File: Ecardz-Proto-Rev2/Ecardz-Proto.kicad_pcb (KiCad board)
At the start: 4 copper layers, 53.2 x 93.2 mm, 66 parts, among them IC1 M24LR04E-RMN6T/2, J2 Conn_01x24, J3 Conn_01x06, Q1 NMOS, U1 STM32L071K8Ux

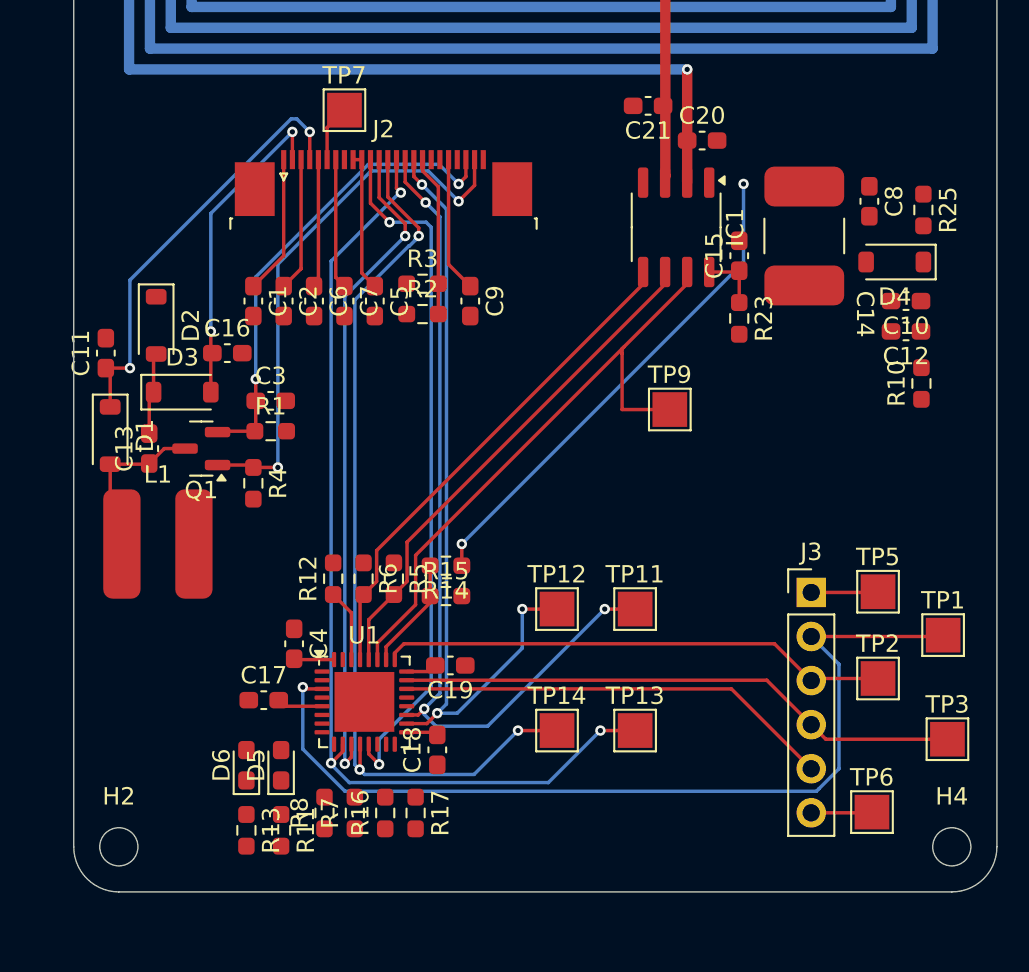
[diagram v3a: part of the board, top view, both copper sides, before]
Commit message: Added traces for everything but gruond layer
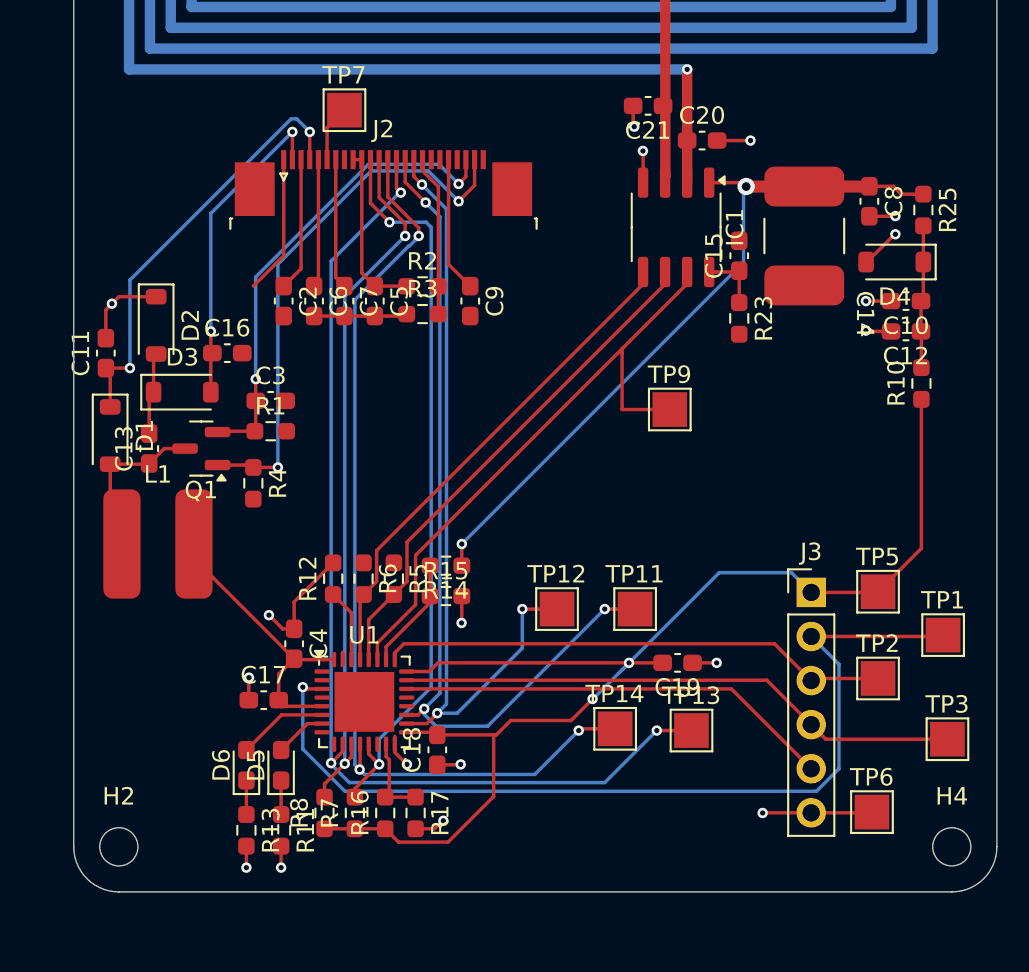
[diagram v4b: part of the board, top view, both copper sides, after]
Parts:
- removed C1: 1uF, Capacitor_SMD:C_0603_1608Metric_Pad1.08x0.95mm_HandSolder
- moved C19 13.1 mm to (193.2, 102.6)
- moved TP14 3.35 mm to (189.6, 106.4)
- moved TP13 3.25 mm to (194.0, 106.5)
- moved R3 1.75 mm to (178.5, 82.5)
- moved R2 1.60 mm to (178.5, 80.9)
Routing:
- net VDD: track 20.1 -> 100.4 mm, vias 0 -> 2
- net GND: track 3.52 -> 50.2 mm, vias 0 -> 18
- net /NFC/V_E_HARVEST: track 28.7 -> 41.3 mm
- net VDD_HARVEST: track 0.00 -> 8.24 mm
- net /STM/INDICATOR_R: track 0.00 -> 5.20 mm
- net /STM/VDD_MEAS: track 0.00 -> 4.97 mm
- net /EINK/CS#: track 51.6 -> 55.0 mm
- net /EINK/D/C#: track 57.2 -> 60.5 mm
- net /STM/INDICATOR_G: track 0.00 -> 2.99 mm
- net /EINK/SDA: track 40.2 -> 42.7 mm
- net /EINK/SCL: track 38.2 -> 40.6 mm
- net Net-(D6-K): track 0.00 -> 1.96 mm
- net Net-(D5-K): track 0.00 -> 1.96 mm
- added copper zone on In1.Cu, net GND

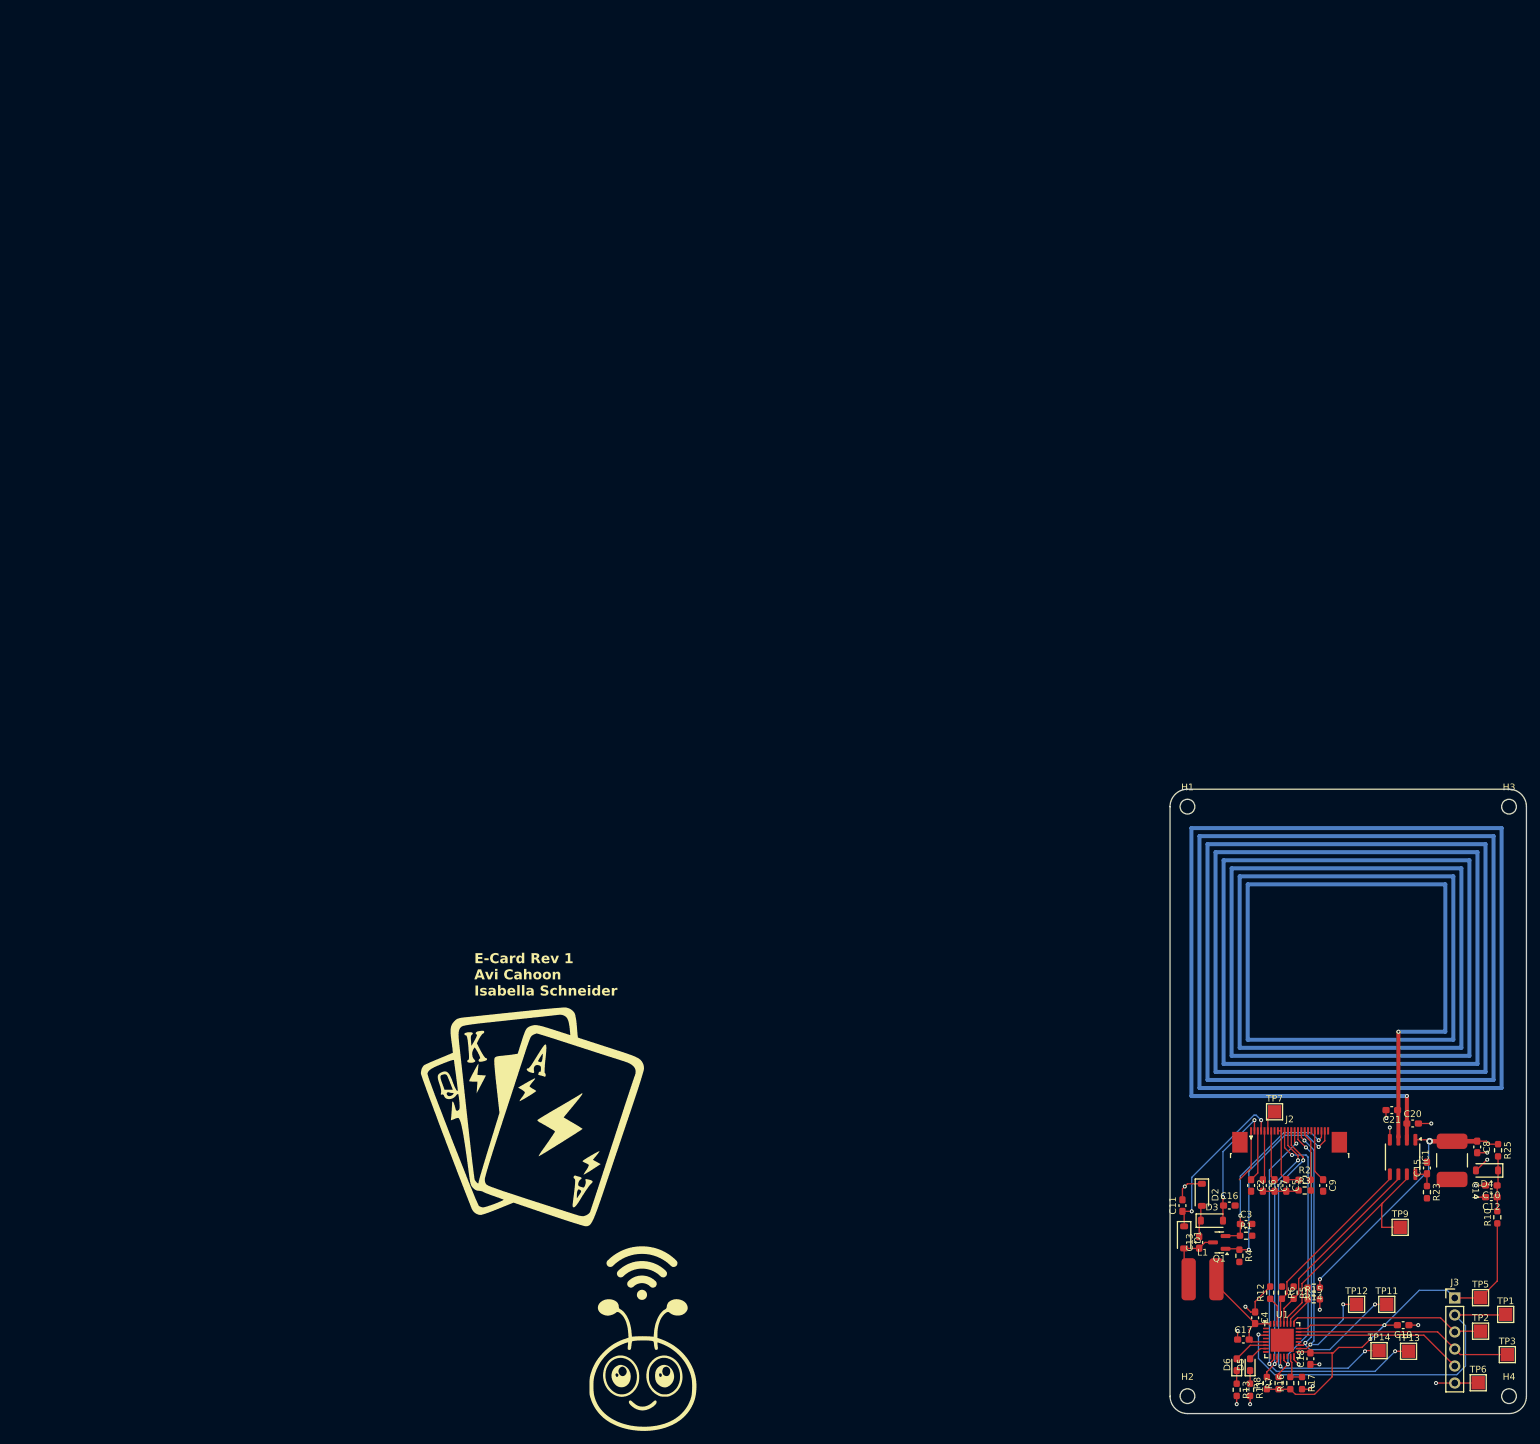
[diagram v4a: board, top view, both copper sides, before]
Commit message: Finished all layout, need to fix inductor and capacitor library
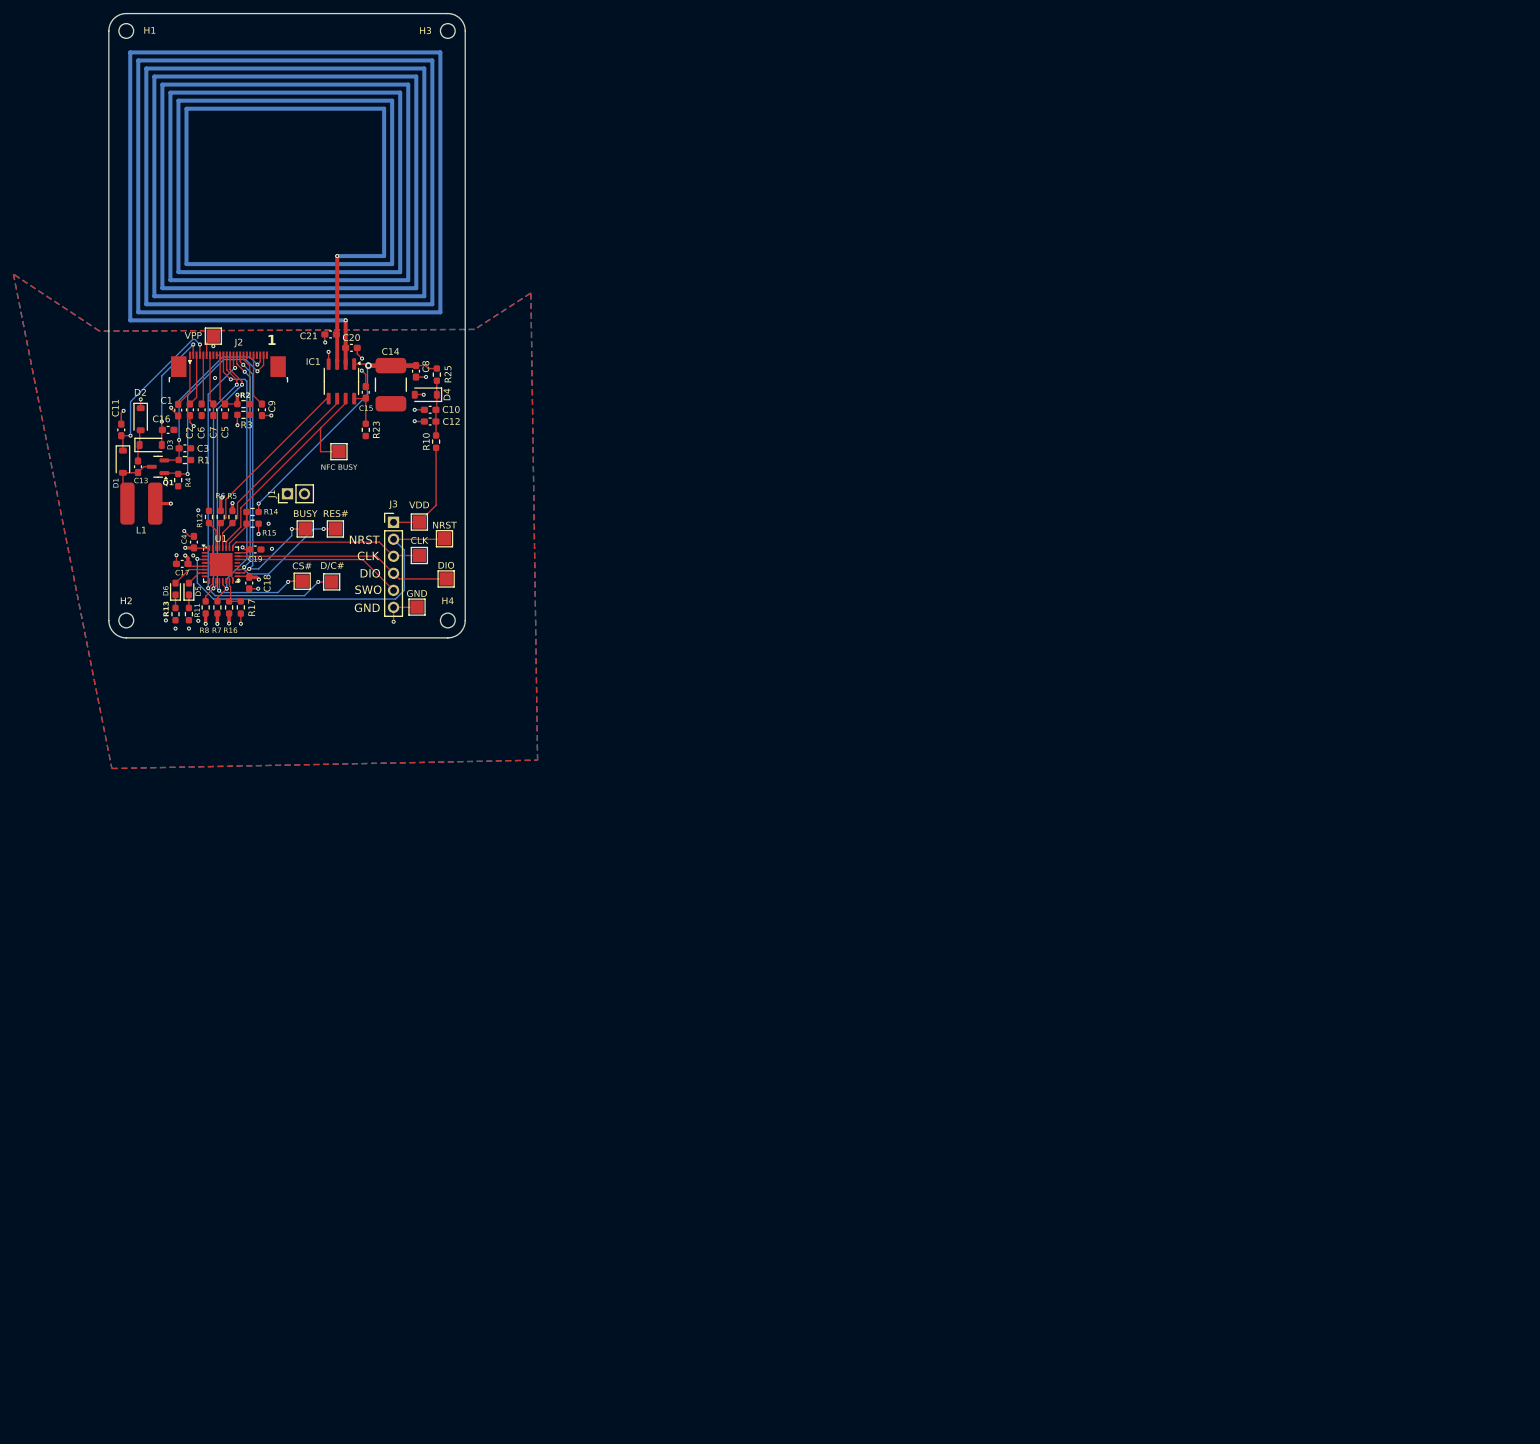
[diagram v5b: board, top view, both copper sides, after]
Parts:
- added C1: 1uF, Capacitor_SMD:C_0603_1608Metric_Pad1.08x0.95mm_HandSolder, F.Cu at (10.3, -34.0)
- added J1: Conn_01x02, Connector_PinHeader_2.54mm:PinHeader_1x02_P2.54mm_Vertical, F.Cu at (26.6, -21.5)
- NFC BUSY: renamed from TP9
- moved C19 206.8 mm to (21.8, -13.2)
- moved CS# 197.6 mm to (28.9, -8.45)
- moved D/C# 197.6 mm to (33.2, -8.35)
- moved C10 196.2 mm to (48.0, -34.0)
- moved C12 196.2 mm to (48.0, -32.3)
- moved C20 196.2 mm to (36.2, -43.3)
- moved D2 196.2 mm to (4.74, -32.6)
- moved D3 196.2 mm to (6.24, -28.8)
- moved IC1 196.2 mm to (34.7, -38.3)
- moved R25 196.2 mm to (49.0, -39.3)
- moved C11 196.2 mm to (1.84, -31.0)
- moved C13 196.2 mm to (4.34, -25.5)
- moved C14 196.2 mm to (42.1, -37.8)
- moved C15 196.2 mm to (38.3, -36.7)
- moved C16 196.2 mm to (8.84, -31.0)
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- renumbered TP12 to BUSY, TP2 to CLK, TP14 to CS#, TP13 to D/C#, TP3 to DIO, TP6 to GND, TP1 to NRST, TP11 to RES#, TP5 to VDD, TP7 to VPP
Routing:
- net VDD: track 100.4 -> 53.1 mm, vias 2 -> 11
- net GND: track 50.2 -> 47.3 mm, vias 18 -> 31
- net /EINK/D/C#: track 60.5 -> 57.8 mm
- net /EINK/CS#: track 55.0 -> 52.3 mm
- net /NFC/VDD_NFC: track 3.60 -> 5.60 mm
- net /EINK/RES#: track 49.6 -> 51.0 mm
- net /EINK/BUSY: track 45.6 -> 46.3 mm
- added copper zone on B.Cu, net GND
- added copper zone on F.Cu, net GND
- added copper zone on In2.Cu, net VDD
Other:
- board text added: "1"
- board text added: "CLK"
- board text added: "DIO"
- board text added: "GND"
- board text added: "NRST"
- board text added: "SWO"
- board text removed: "E-Card Rev 1 Avi Cahoon Isabella Schneider"

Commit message: final schematic
final schematic done and BOM generated except for pogo pins and capacitors
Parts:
- removed the C8 at (45.8, -39.8)
- added C22: TBD, parts-lib:C_2917, F.Cu at (46.5, -38.0)
- added C23: TBD, Capacitor_SMD:C_0805_2012Metric_Pad1.18x1.45mm_HandSolder, F.Cu at (34.8, -40.2)
- added C8: TBD, Capacitor_SMD:C_0805_2012Metric_Pad1.18x1.45mm_HandSolder, F.Cu at (51.8, -31.0)
- added C8: TBD, Capacitor_SMD:C_0805_2012Metric_Pad1.18x1.45mm_HandSolder, F.Cu at (49.5, -23.0)
- added C8: TBD, Capacitor_SMD:C_0805_2012Metric_Pad1.18x1.45mm_HandSolder, F.Cu at (40.5, -23.0)
- added C8: TBD, Capacitor_SMD:C_0805_2012Metric_Pad1.18x1.45mm_HandSolder, F.Cu at (47.2, -23.0)
- added C8: TBD, Capacitor_SMD:C_0805_2012Metric_Pad1.18x1.45mm_HandSolder, F.Cu at (40.2, -44.2)
- added C8: TBD, Capacitor_SMD:C_0805_2012Metric_Pad1.18x1.45mm_HandSolder, F.Cu at (51.5, -44.2)
- added C8: TBD, Capacitor_SMD:C_0805_2012Metric_Pad1.18x1.45mm_HandSolder, F.Cu at (36.0, -27.0)
- added C8: TBD, Capacitor_SMD:C_0805_2012Metric_Pad1.18x1.45mm_HandSolder, F.Cu at (49.5, -27.0)
- added C8: TBD, Capacitor_SMD:C_0805_2012Metric_Pad1.18x1.45mm_HandSolder, F.Cu at (47.2, -27.0)
- added C8: TBD, Capacitor_SMD:C_0805_2012Metric_Pad1.18x1.45mm_HandSolder, F.Cu at (51.8, -27.0)
- added C8: TBD, Capacitor_SMD:C_0805_2012Metric_Pad1.18x1.45mm_HandSolder, F.Cu at (51.0, -41.0)
- added C8: TBD, Capacitor_SMD:C_0805_2012Metric_Pad1.18x1.45mm_HandSolder, F.Cu at (45.0, -27.0)
- added C8: TBD, Capacitor_SMD:C_0805_2012Metric_Pad1.18x1.45mm_HandSolder, F.Cu at (35.8, -44.2)
- added C8: TBD, Capacitor_SMD:C_0805_2012Metric_Pad1.18x1.45mm_HandSolder, F.Cu at (38.2, -31.0)
- added C8: TBD, Capacitor_SMD:C_0805_2012Metric_Pad1.18x1.45mm_HandSolder, F.Cu at (42.8, -31.0)
- added C8: TBD, Capacitor_SMD:C_0805_2012Metric_Pad1.18x1.45mm_HandSolder, F.Cu at (51.0, -36.5)
- added C8: TBD, Capacitor_SMD:C_0805_2012Metric_Pad1.18x1.45mm_HandSolder, F.Cu at (42.8, -27.0)
- added C8: TBD, Capacitor_SMD:C_0805_2012Metric_Pad1.18x1.45mm_HandSolder, F.Cu at (49.2, -44.2)
- added C8: TBD, Capacitor_SMD:C_0805_2012Metric_Pad1.18x1.45mm_HandSolder, F.Cu at (40.5, -31.0)
- added C8: TBD, Capacitor_SMD:C_0805_2012Metric_Pad1.18x1.45mm_HandSolder, F.Cu at (51.8, -23.0)
- added C8: TBD, Capacitor_SMD:C_0805_2012Metric_Pad1.18x1.45mm_HandSolder, F.Cu at (36.0, -31.0)
- added C8: TBD, Capacitor_SMD:C_0805_2012Metric_Pad1.18x1.45mm_HandSolder, F.Cu at (42.5, -44.2)
- added C8: TBD, Capacitor_SMD:C_0805_2012Metric_Pad1.18x1.45mm_HandSolder, F.Cu at (45.0, -31.0)
- added C8: TBD, Capacitor_SMD:C_0805_2012Metric_Pad1.18x1.45mm_HandSolder, F.Cu at (47.0, -44.2)
- added C8: TBD, Capacitor_SMD:C_0805_2012Metric_Pad1.18x1.45mm_HandSolder, F.Cu at (44.8, -44.2)
- added C8: TBD, Capacitor_SMD:C_0805_2012Metric_Pad1.18x1.45mm_HandSolder, F.Cu at (51.0, -38.8)
- added C8: TBD, Capacitor_SMD:C_0805_2012Metric_Pad1.18x1.45mm_HandSolder, F.Cu at (49.5, -31.0)
- added C8: TBD, Capacitor_SMD:C_0805_2012Metric_Pad1.18x1.45mm_HandSolder, F.Cu at (40.5, -27.0)
- added C8: TBD, Capacitor_SMD:C_0805_2012Metric_Pad1.18x1.45mm_HandSolder, F.Cu at (45.0, -23.0)
- added C8: TBD, Capacitor_SMD:C_0805_2012Metric_Pad1.18x1.45mm_HandSolder, F.Cu at (51.0, -34.2)
- added C8: TBD, Capacitor_SMD:C_0805_2012Metric_Pad1.18x1.45mm_HandSolder, F.Cu at (33.8, -27.0)
- added C8: TBD, Capacitor_SMD:C_0805_2012Metric_Pad1.18x1.45mm_HandSolder, F.Cu at (47.2, -31.0)
- added C8: TBD, Capacitor_SMD:C_0805_2012Metric_Pad1.18x1.45mm_HandSolder, F.Cu at (38.2, -27.0)
- added C8: TBD, Capacitor_SMD:C_0805_2012Metric_Pad1.18x1.45mm_HandSolder, F.Cu at (38.0, -44.2)
- added C8: TBD, Capacitor_SMD:C_0805_2012Metric_Pad1.18x1.45mm_HandSolder, F.Cu at (42.8, -23.0)
- added R18: 0R, Resistor_SMD:R_0603_1608Metric_Pad0.98x0.95mm_HandSolder, F.Cu at (31.8, -27.0)
- added R19: 0R, Resistor_SMD:R_0603_1608Metric_Pad0.98x0.95mm_HandSolder, F.Cu at (39.8, -19.6)
- added R9: 0R, Resistor_SMD:R_0603_1608Metric_Pad0.98x0.95mm_HandSolder, F.Cu at (37.5, -41.0)
- TP9: renamed from NFC BUSY
- moved R25 23.3 mm to (32.0, -23.2)
- moved D4 20.6 mm to (34.0, -20.5), turned to -90 degrees
- moved C10 17.5 mm to (36.2, -21.0), turned to -90 degrees
- moved R10 15.9 mm to (38.5, -17.2), turned to 180 degrees
- moved C12 15.0 mm to (38.0, -21.0), turned to -90 degrees
- moved TP9 6.04 mm to (28.8, -25.5)
- moved R23 5.47 mm to (33.0, -32.2)
- moved C15 3.70 mm to (34.6, -36.7)
- moved C20 3.70 mm to (32.5, -43.3)
- moved C21 3.70 mm to (29.4, -45.3)
- moved IC1 3.70 mm to (31.0, -38.3)
- moved C14 0.63 mm to (41.5, -38.0)
- renumbered NRST to TP1, RES# to TP11, BUSY to TP12, D/C# to TP13, CS# to TP14, CLK to TP2, DIO to TP3, VDD to TP5, GND to TP6, VPP to TP7
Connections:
- C14 pad 1: /NFC/V_E_HARVEST -> /NFC/NFC_BULK_CAP
- R25 pad 1: /NFC/V_E_HARVEST -> Net-(R18-Pad2)
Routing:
- net /NFC/V_E_HARVEST: track 41.3 -> 26.0 mm
- net GND: track 47.3 -> 33.7 mm, vias 31 -> 65
- net VDD: track 53.1 -> 40.9 mm
- net VDD_HARVEST: track 8.24 -> 0.00 mm
- net /STM/NFC_BUSY: track 36.2 -> 28.3 mm
- net /STM/I2C_NFC_SDA: track 29.3 -> 27.6 mm
- net /STM/I2C_NFC_SCL: track 29.4 -> 27.9 mm
- net /NFC/VDD_NFC: track 5.60 -> 5.06 mm
